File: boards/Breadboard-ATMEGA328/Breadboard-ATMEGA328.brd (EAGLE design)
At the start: 15.2 x 44.5 mm, 10 parts, among them IC1 ATMEGA328P-PU, J1 PINHD-1X7, J2 PINHD-1X7, J3 PINHD-1X7, J4 PINHD-1X7

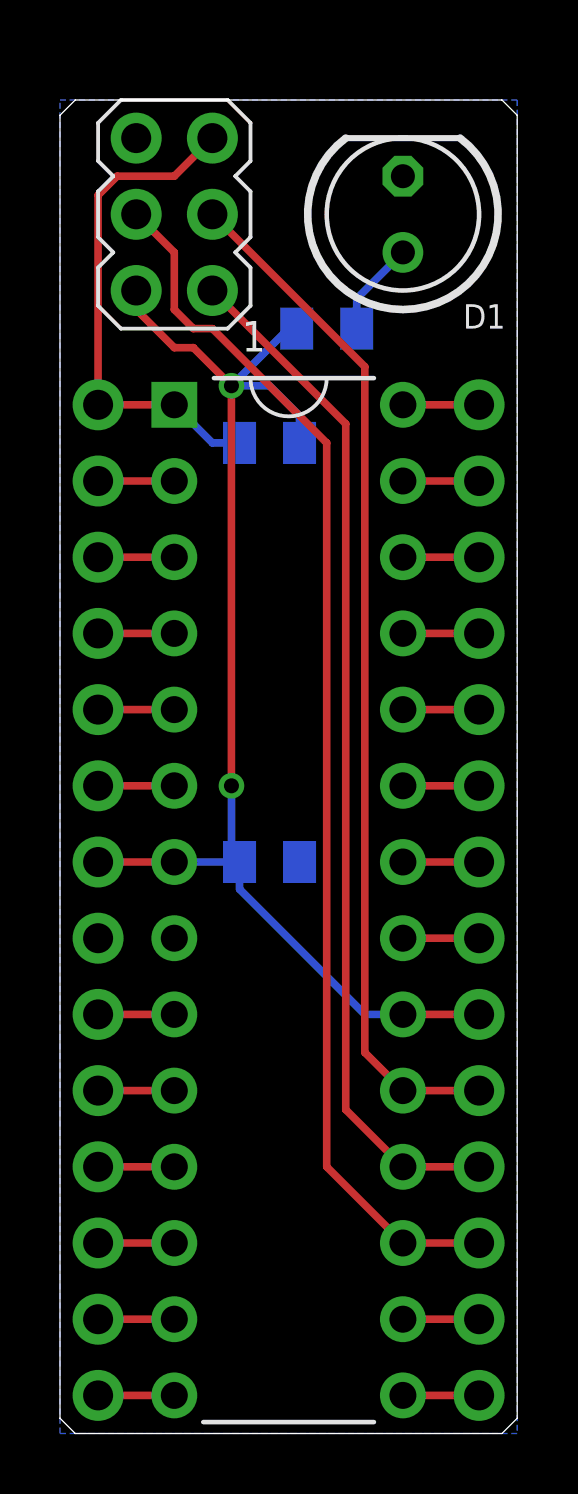
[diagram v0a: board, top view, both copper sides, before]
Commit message: Updated breadboard ATMega328
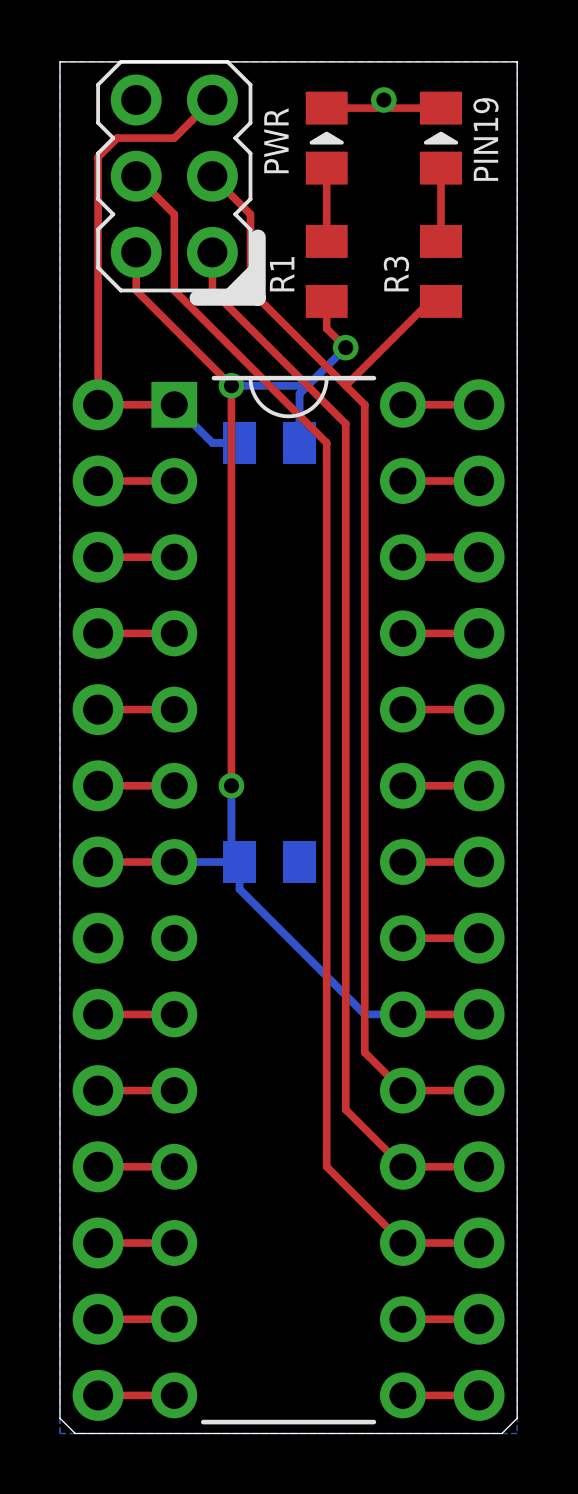
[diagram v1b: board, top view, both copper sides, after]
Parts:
- added D2: LED-0805, SaintGimp:LED-0805
- added R3: 330R, SaintGimp:RESISTOR-0805
- D1: value LED -> LED-0805; device SaintGimp:LED5MM -> SaintGimp:LED-0805
- moved D1 3.59 mm to (8.89, 43.2)
- moved R1 1.91 mm to (8.89, 38.7), flipped to the top, turned to 90 degrees
- moved ISP1 1.27 mm to (3.81, 41.9)
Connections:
- new net N$8: D2.1, R3.2
- net GND: now also D1.2, D2.2; no longer D1.K
- net N$7: now also D1.1; no longer D1.A
- net SCK: now also R3.1
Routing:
- net SCK: track 34.4 -> 40.0 mm
- net GND: track 0.00 -> 4.03 mm, vias 0 -> 1
- net VCC: track 42.7 -> 45.2 mm, vias 2 -> 3
- net N$8: track 0.00 -> 2.45 mm
- net RST: track 16.8 -> 18.1 mm
- net MISO: track 34.4 -> 35.7 mm
- net MOSI: track 40.9 -> 41.8 mm
- net N$7: track 3.18 -> 2.45 mm
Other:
- board size 15.2 x 44.5 mm -> 15.2 x 45.7 mm
- board text added: "PIN19"
- board text added: "PWR"
- board text added: "v1.1"
- board text removed: "v1.0"
